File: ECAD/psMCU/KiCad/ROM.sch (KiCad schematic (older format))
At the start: 36 parts, among them J1 Prog, SW11 Slot Select, U100 SST39SF010A-55-4C-WHE, U103 SN74HC165PW, U104 SN74HC165PW, U248 SN74HC595PW, U409 SN74LVC1G125DCK, U52 SN74LVC1G04DCK, U89 SN74HC595PW, U90 SN74HC595PW, U92 SN74HC245PW, U93 SN74HC245PW, U97 SN74HC595PW, U98 SN74HC595PW, U99 SST39SF010A-55-4C-WHE

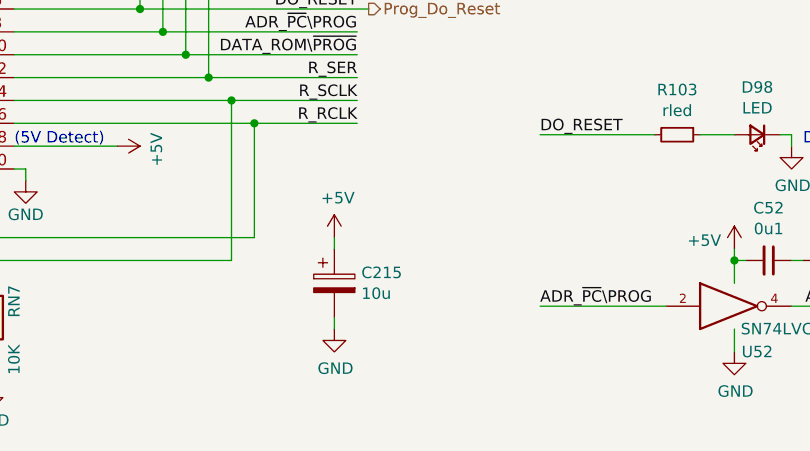
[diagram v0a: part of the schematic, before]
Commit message: Sch: Removed Regulator, Added extra spread bulk C
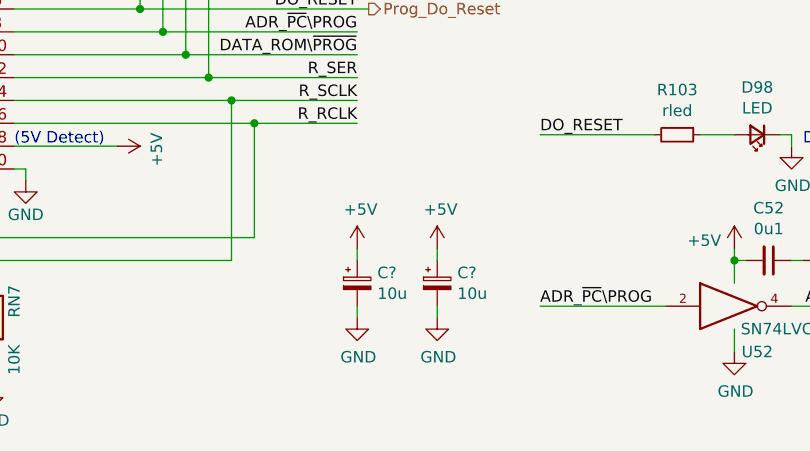
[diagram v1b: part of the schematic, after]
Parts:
- removed C215: 10u, Capacitor_SMD:CP_Elec_6.3x7.7, symbol Device:CP
- added C? (x2): 10u, symbol Device:CP_Small
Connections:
- net +5V: now also C?.1, C?.1
- net GND: now also C?.2, C?.2
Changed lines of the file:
@@
 	2750 15300 3800 15300
-$Comp
-L Device:CP C?
-U 1 1 60DF3937
-P 4250 15400
-AR Path="/60DF3937" Ref="C?"  Part="1"
-AR Path="/62043340/60DF3937" Ref="C?"  Part="1"
-AR Path="/5F28170E/60DF3937" Ref="C215"  Part="1"
-F 0 "C215" H 4368 15446 50  0000 L CNN
-F 1 "10u" H 4368 15355 50  0000 L CNN
-F 2 "Capacitor_SMD:CP_Elec_6.3x7.7" H 4288 15250 50  0001 C CNN
-F 3 "~" H 4250 15400 50  0001 C CNN
-	1    4250 15400
-	1    0    0    -1
-$EndComp
-$Comp
-L power:GND #PWR?
-U 1 1 60DF3940
-P 4250 15600
-AR Path="/60DF3940" Ref="#PWR?"  Part="1"
-AR Path="/62043340/60DF3940" Ref="#PWR?"  Part="1"
-AR Path="/5F28170E/60DF3940" Ref="#PWR0392"  Part="1"
-F 0 "#PWR0392" H 4250 15350 50  0001 C CNN
-F 1 "GND" H 4255 15427 50  0000 C CNN
-F 2 "" H 4250 15600 50  0001 C CNN
-F 3 "" H 4250 15600 50  0001 C CNN
-	1    4250 15600
-	1    0    0    -1
-$EndComp
-$Comp
-L power:+5V #PWR?
-U 1 1 60DF3947
-P 4250 15200
-AR Path="/60DF3947" Ref="#PWR?"  Part="1"
-AR Path="/62043340/60DF3947" Ref="#PWR?"  Part="1"
-AR Path="/5F28170E/60DF3947" Ref="#PWR0431"  Part="1"
-F 0 "#PWR0431" H 4250 15050 50  0001 C CNN
-F 1 "+5V" H 4265 15373 50  0000 C CNN
-F 2 "" H 4250 15200 50  0001 C CNN
-F 3 "" H 4250 15200 50  0001 C CNN
-	1    4250 15200
-	1    0    0    -1
-$EndComp
-Wire Wire Line
-	4250 15200 4250 15250
-Wire Wire Line
-	4250 15550 4250 15600
 $Comp
 L power:+5V #PWR0779
@@
 Wire Wire Line
 	7000 10850 7000 10350
+$Comp
+L Device:CP_Small C?
+U 1 1 62617304
+P 4700 15400
+AR Path="/62043340/62617304" Ref="C?"  Part="1"
+AR Path="/5FD6B215/62617304" Ref="C?"  Part="1"
+F 0 "C?" H 4788 15446 50  0000 L CNN
+F 1 "10u" H 4788 15355 50  0000 L CNN
+F 2 "" H 4700 15400 50  0001 C CNN
+F 3 "~" H 4700 15400 50  0001 C CNN
+	1    4700 15400
+	1    0    0    -1
+$EndComp
+$Comp
+L power:GND #PWR?
+U 1 1 6261730A
+P 4700 15550
+AR Path="/6261730A" Ref="#PWR?"  Part="1"
+AR Path="/62043340/6261730A" Ref="#PWR?"  Part="1"
+AR Path="/5FD6B215/6261730A" Ref="#PWR?"  Part="1"
+F 0 "#PWR?" H 4700 15300 50  0001 C CNN
+F 1 "GND" H 4705 15377 50  0000 C CNN
+F 2 "" H 4700 15550 50  0001 C CNN
+F 3 "" H 4700 15550 50  0001 C CNN
+	1    4700 15550
+	1    0    0    -1
+$EndComp
+Wire Wire Line
+	4700 15550 4700 15500
+Wire Wire Line
+	4700 15250 4700 15300
+$Comp
+L power:+5V #PWR?
+U 1 1 62617312
+P 4700 15250
+AR Path="/62617312" Ref="#PWR?"  Part="1"
+AR Path="/62043340/62617312" Ref="#PWR?"  Part="1"
+AR Path="/5FD6B215/62617312" Ref="#PWR?"  Part="1"
+F 0 "#PWR?" H 4700 15100 50  0001 C CNN
+F 1 "+5V" H 4715 15423 50  0000 C CNN
+F 2 "" H 4700 15250 50  0001 C CNN
+F 3 "" H 4700 15250 50  0001 C CNN
+	1    4700 15250
+	1    0    0    -1
+$EndComp
+$Comp
+L Device:CP_Small C?
+U 1 1 626890F5
+P 4350 15400
+AR Path="/62043340/626890F5" Ref="C?"  Part="1"
+AR Path="/5FD6B215/626890F5" Ref="C?"  Part="1"
+F 0 "C?" H 4438 15446 50  0000 L CNN
+F 1 "10u" H 4438 15355 50  0000 L CNN
+F 2 "" H 4350 15400 50  0001 C CNN
+F 3 "~" H 4350 15400 50  0001 C CNN
+	1    4350 15400
+	1    0    0    -1
+$EndComp
+$Comp
+L power:GND #PWR?
+U 1 1 626890FB
+P 4350 15550
+AR Path="/626890FB" Ref="#PWR?"  Part="1"
+AR Path="/62043340/626890FB" Ref="#PWR?"  Part="1"
+AR Path="/5FD6B215/626890FB" Ref="#PWR?"  Part="1"
+F 0 "#PWR?" H 4350 15300 50  0001 C CNN
+F 1 "GND" H 4355 15377 50  0000 C CNN
+F 2 "" H 4350 15550 50  0001 C CNN
+F 3 "" H 4350 15550 50  0001 C CNN
+	1    4350 15550
+	1    0    0    -1
+$EndComp
+Wire Wire Line
+	4350 15550 4350 15500
+Wire Wire Line
+	4350 15250 4350 15300
+$Comp
+L power:+5V #PWR?
+U 1 1 62689103
+P 4350 15250
+AR Path="/62689103" Ref="#PWR?"  Part="1"
+AR Path="/62043340/62689103" Ref="#PWR?"  Part="1"
+AR Path="/5FD6B215/62689103" Ref="#PWR?"  Part="1"
+F 0 "#PWR?" H 4350 15100 50  0001 C CNN
+F 1 "+5V" H 4365 15423 50  0000 C CNN
+F 2 "" H 4350 15250 50  0001 C CNN
+F 3 "" H 4350 15250 50  0001 C CNN
+	1    4350 15250
+	1    0    0    -1
+$EndComp
 Wire Bus Line
 	2800 4200 2800 5500

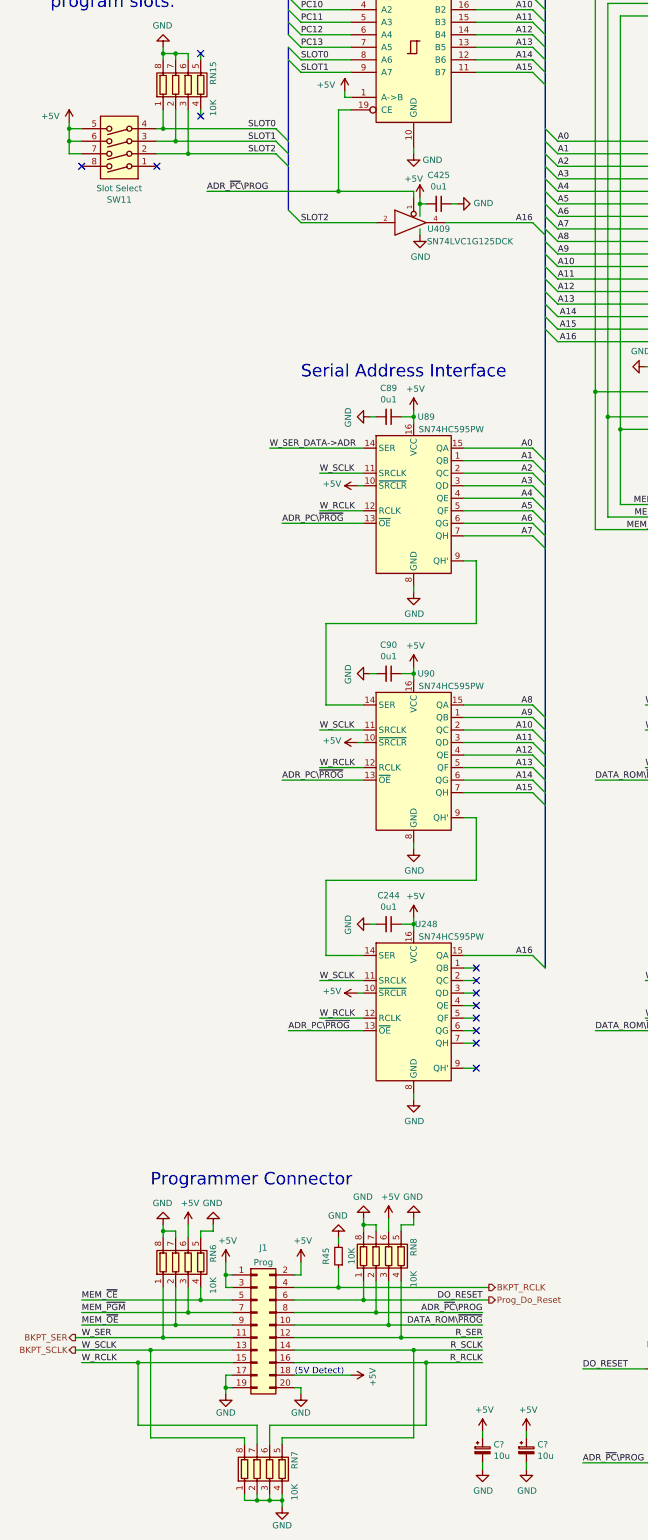
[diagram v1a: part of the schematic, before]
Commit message: Sch: Reworked Peripheral Interface (Buffers)
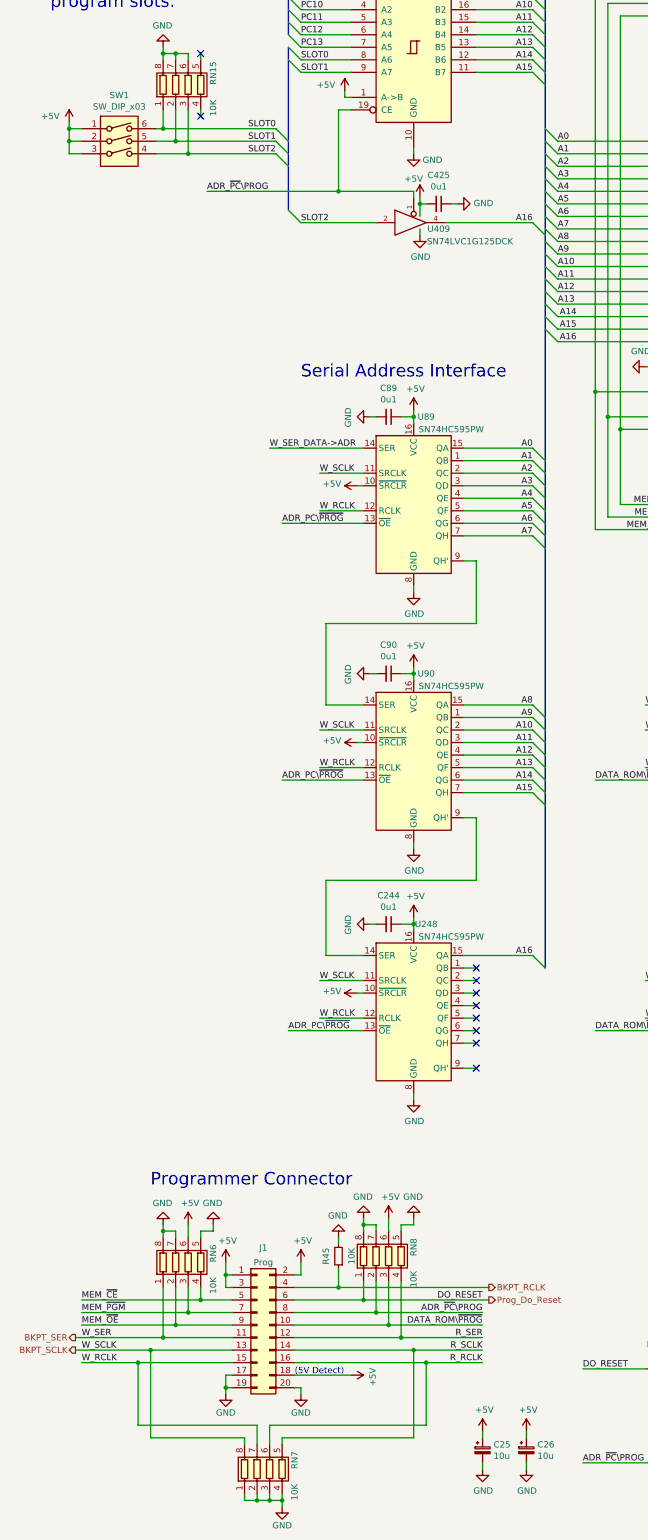
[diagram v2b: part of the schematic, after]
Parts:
- removed SW11: Slot Select, Button_Switch_SMD:SW_DIP_SPSTx04_Slide_KingTek_DSHP04TJ_W5.25mm_P1.27mm_JPin, symbol Switch:SW_DIP_x04
- added SW1: SW_DIP_x03, symbol Switch:SW_DIP_x03
- gave numbers to parts that had none: 2
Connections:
- net +5V: now also SW1.1, SW1.2, SW1.3
- net SLOT0: now also SW1.6
- net SLOT1: now also SW1.5
- net SLOT2: now also SW1.4
- no-connect marks 14 -> 12
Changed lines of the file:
@@
 $Descr A3 11693 16535 portrait
 encoding utf-8
-Sheet 28 97
+Sheet 28 96
 Title "psMCU"
 Date "2022-02-13"
@@
 Entry Wire Line
 	4750 5600 4850 5700
-$Comp
-L Switch:SW_DIP_x04 SW11
-U 1 1 60B1A0E4
-P 1450 4950
-F 0 "SW11" H 1450 5417 50  0000 C CNN
-F 1 "Slot Select" H 1450 5326 50  0000 C CNN
-F 2 "Button_Switch_SMD:SW_DIP_SPSTx04_Slide_KingTek_DSHP04TJ_W5.25mm_P1.27mm_JPin" H 1450 4950 50  0001 C CNN
-F 3 "~" H 1450 4950 50  0001 C CNN
-	1    1450 4950
-	-1   0    0    1
-$EndComp
 Wire Wire Line
 	1150 4850 1050 4850
@@
 Wire Wire Line
 	1700 15300 2450 15300
-NoConn ~ 1150 5150
-NoConn ~ 1750 5150
 Wire Wire Line
 	1150 14700 1600 14700
@@
 AR Path="/62043340/62617304" Ref="C?"  Part="1"
 AR Path="/5FD6B215/62617304" Ref="C?"  Part="1"
-F 0 "C?" H 4788 15446 50  0000 L CNN
+AR Path="/5F28170E/62617304" Ref="C26"  Part="1"
+F 0 "C26" H 4788 15446 50  0000 L CNN
 F 1 "10u" H 4788 15355 50  0000 L CNN
 F 2 "" H 4700 15400 50  0001 C CNN
@@
 AR Path="/62043340/6261730A" Ref="#PWR?"  Part="1"
 AR Path="/5FD6B215/6261730A" Ref="#PWR?"  Part="1"
-F 0 "#PWR?" H 4700 15300 50  0001 C CNN
+AR Path="/5F28170E/6261730A" Ref="#PWR0123"  Part="1"
+F 0 "#PWR0123" H 4700 15300 50  0001 C CNN
 F 1 "GND" H 4705 15377 50  0000 C CNN
 F 2 "" H 4700 15550 50  0001 C CNN
@@
 AR Path="/62043340/62617312" Ref="#PWR?"  Part="1"
 AR Path="/5FD6B215/62617312" Ref="#PWR?"  Part="1"
-F 0 "#PWR?" H 4700 15100 50  0001 C CNN
+AR Path="/5F28170E/62617312" Ref="#PWR0124"  Part="1"
+F 0 "#PWR0124" H 4700 15100 50  0001 C CNN
 F 1 "+5V" H 4715 15423 50  0000 C CNN
 F 2 "" H 4700 15250 50  0001 C CNN
@@
 AR Path="/62043340/626890F5" Ref="C?"  Part="1"
 AR Path="/5FD6B215/626890F5" Ref="C?"  Part="1"
-F 0 "C?" H 4438 15446 50  0000 L CNN
+AR Path="/5F28170E/626890F5" Ref="C25"  Part="1"
+F 0 "C25" H 4438 15446 50  0000 L CNN
 F 1 "10u" H 4438 15355 50  0000 L CNN
 F 2 "" H 4350 15400 50  0001 C CNN
@@
 AR Path="/62043340/626890FB" Ref="#PWR?"  Part="1"
 AR Path="/5FD6B215/626890FB" Ref="#PWR?"  Part="1"
-F 0 "#PWR?" H 4350 15300 50  0001 C CNN
+AR Path="/5F28170E/626890FB" Ref="#PWR0125"  Part="1"
+F 0 "#PWR0125" H 4350 15300 50  0001 C CNN
 F 1 "GND" H 4355 15377 50  0000 C CNN
 F 2 "" H 4350 15550 50  0001 C CNN
@@
 AR Path="/62043340/62689103" Ref="#PWR?"  Part="1"
 AR Path="/5FD6B215/62689103" Ref="#PWR?"  Part="1"
-F 0 "#PWR?" H 4350 15100 50  0001 C CNN
+AR Path="/5F28170E/62689103" Ref="#PWR0126"  Part="1"
+F 0 "#PWR0126" H 4350 15100 50  0001 C CNN
 F 1 "+5V" H 4365 15423 50  0000 C CNN
 F 2 "" H 4350 15250 50  0001 C CNN
@@
 Wire Bus Line
 	7750 1650 7750 12550
+$Comp
+L Switch:SW_DIP_x03 SW1
+U 1 1 62141836
+P 1450 5050
+F 0 "SW1" H 1450 5517 50  0000 C CNN
+F 1 "SW_DIP_x03" H 1450 5426 50  0000 C CNN
+F 2 "" H 1450 5050 50  0001 C CNN
+F 3 "~" H 1450 5050 50  0001 C CNN
+	1    1450 5050
+	1    0    0    -1
+$EndComp
 $EndSCHEMATC

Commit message: Sch: Implemented much improved debugger interface
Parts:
- removed C25, C26: 10u, symbol Device:CP_Small
- removed D98: LED, NoRef_Footprints:D_0603_1608Metric_NoRef, symbol Device:LED_Small
- removed J1: Prog, Connector_IDC:IDC-Header_2x10_P2.54mm_Vertical, symbol Connector_Generic:Conn_02x10_Odd_Even
- removed R103: rled, NoRef_Footprints:R_0603_1608Metric_NoRef, symbol Device:R_Small
- removed R45: 10K, NoRef_Footprints:R_0603_1608Metric_NoRef, symbol Device:R_Small
- removed RN6, RN7, RN8: 10K, NoRef_Footprints:R_Array_Convex_4x0603_NoRef, symbol Device:R_Pack04
- added C219, C222, C223: 0u1, NoRef_Footprints:C_0603_1608Metric_NoRef, symbol Device:C_Small
- added U221: 74HC594PW, Package_SO:TSSOP-16_4.4x5mm_P0.65mm, symbol 74HC594:75HC594
- added U236, U238: SN74LVC1G04DCK, Package_TO_SOT_SMD:SOT-353_SC-70-5, symbol 74xGxx:74LVC1G04
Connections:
- net +5V: now also C219.1, C222.2, C223.2, U221.16 (Vcc), U236.5 (VCC), U238.5 (VCC)
- net ADR_~PC~\PROG: now also U221.3 (Q3)
- net DATA_ROM\~PROG~: now also U238.4
- net GND: now also C219.2, C222.1, C223.1, U221.8 (GND), U236.3 (GND), U238.3 (GND); no longer U103.10 (DS)
- net MEM_~CE: now also U221.2 (Q2)
- net MEM_~OE: now also U221.15 (Q0)
- net MEM_~PGM: now also U236.4
- net BKPT_SCLK renamed DBGW_SCLK
- net DBGW_SCLK: now also U221.11 (SHCP)
- net BKPT_SER renamed DBGW_SER
- net DBGW_SER: now also U221.14 (DS)
- net R_RCLK renamed DBGR_RCLK
- net R_SCLK renamed DBGR_SCLK
- net R_SER renamed DBGR_SER_O
- net W_RCLK renamed DBGW_ROM
- new net DATA_~ROM~\PROG: U221.4 (Q4), U238.2
- new net DBGR_SER_I: U103.10 (DS)
- new net DBGW_ROMCT: U221.12 (STCP)
- new net MEM_PGM: U221.1 (Q1), U236.2
- new net ~PWR_RESET: U221.10 (~SHR), U221.13 (~STR)
- no-connect marks 12 -> 16
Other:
- note added: "Control Signal Interface"
- note removed: "(5V Detect)"
- note removed: "Do Reset"
- note removed: "Programmer Connector"
- moved on the sheet: C52, U52

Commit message: Sch: Cleanup + Small fixes
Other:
- note added: "Debugger Address Output"
- note added: "Debugger Control Signal Output"
- note added: "Debugger Data Input"
- note added: "Debugger Data Output"
- note added: "Program Counter Disconnect"
- note added: "Used during programming."
- note removed: "Control Signal Interface"
- note removed: "Disconnect Program Counter\nwhile programming."
- note removed: "Serial Address Interface"
- note removed: "Serial Data\nInterface (Reading)"
- note removed: "Serial Data\nInterface (Writing)"
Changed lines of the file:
@@
 $Descr A3 11693 16535 portrait
 encoding utf-8
-Sheet 4 109
+Sheet 65 109
 Title "psMCU"
 Date "2022-02-13"
@@
 Wire Wire Line
 	2650 7400 3400 7400
-Text Notes 2800 1000 0    100  ~ 0
-Disconnect Program Counter\nwhile programming.
-Text Notes 6100 1000 0    100  ~ 0
+Text Notes 2800 850  0    100  ~ 0
+Program Counter Disconnect
+Text Notes 6100 850  0    100  ~ 0
 Memory
-Text Notes 2900 6850 0    100  ~ 0
-Serial Address Interface
+Text Notes 2800 6750 0    100  ~ 0
+Debugger Address Output
 Wire Wire Line
 	3250 4550 3250 4600
-Text Notes 5800 8800 0    100  ~ 0
-Serial Data\nInterface (Writing)
-Text Notes 8850 6600 0    100  ~ 0
-Serial Data\nInterface (Reading)
+Text Notes 8650 6650 0    100  ~ 0
+Debugger Data Input
 Text Label 4750 4300 2    50   ~ 0
 A14
@@
 Wire Wire Line
 	3500 13550 3450 13550
-Text Notes 2900 13150 0    100  ~ 0
-Control Signal Interface
 Text Label 4900 13850 2    50   ~ 0
 MEM_~OE
@@
 NoConn ~ 4250 14550
 NoConn ~ 4250 14650
+Text Notes 3400 1000 0    50   ~ 0
+Used during programming.
+Text Notes 5500 8800 0    100  ~ 0
+Debugger Data Output
+Text Notes 2650 13150 0    100  ~ 0
+Debugger Control Signal Output
 Wire Bus Line
 	2800 4200 2800 5500
